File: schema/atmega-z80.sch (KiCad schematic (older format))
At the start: 68 parts, among them J1 USB Connector, J2 Programmer ISP 10, J3 SPI Connector, J4 I2C Connector, Q1 PNP_2N4403, Q2 PNP_2N4403, Q3 NPN_2N4401, Q4 PNP_2N4403, U1 Z84C0010PEG, U2 ATmega324A-PU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

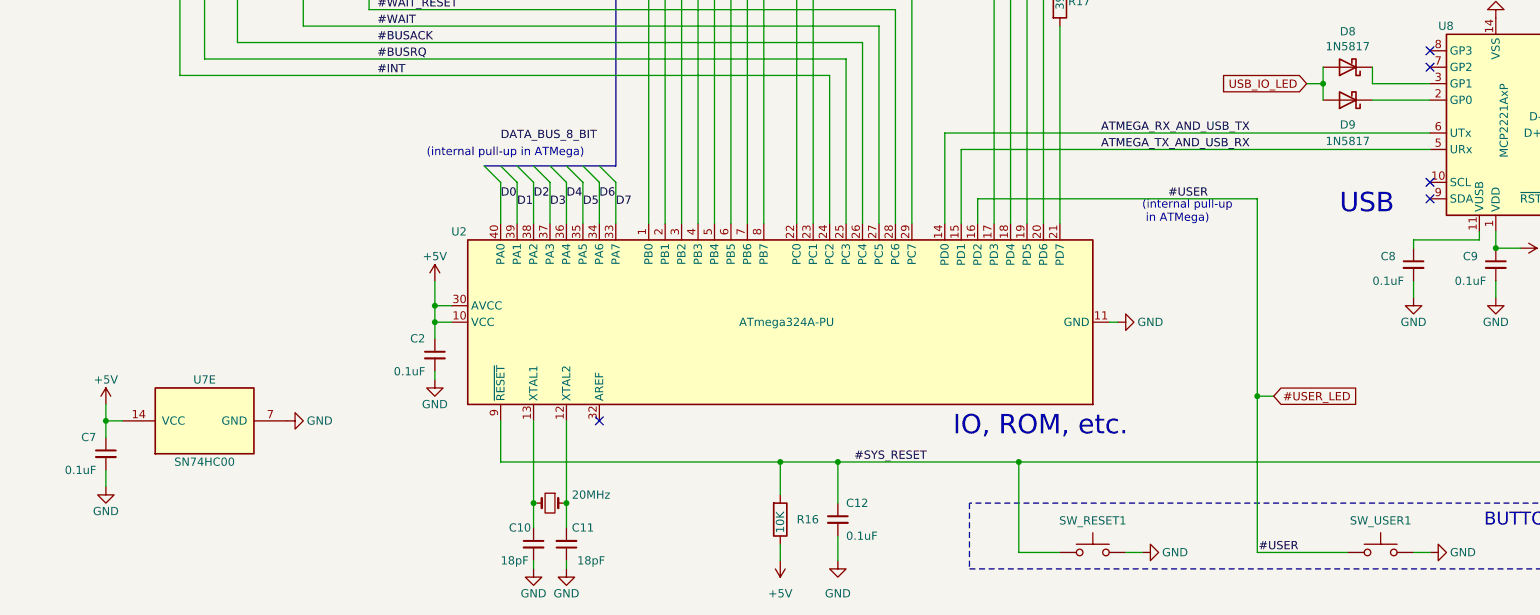
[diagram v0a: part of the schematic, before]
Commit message: A bunch of improvements / additions (#5)
* A bunch of improvements / additions
- PCB layout improvements
- 1N5817 diode datasheet
- CMake support
- ATMega program loader firmware
- program loader tool (z80_prog_loader.py)
- Z80 bootloader (bootloader.asm)
- Z80 sample program (blinky.asm)
- goose logo! (goose-icon.kicad_mod)
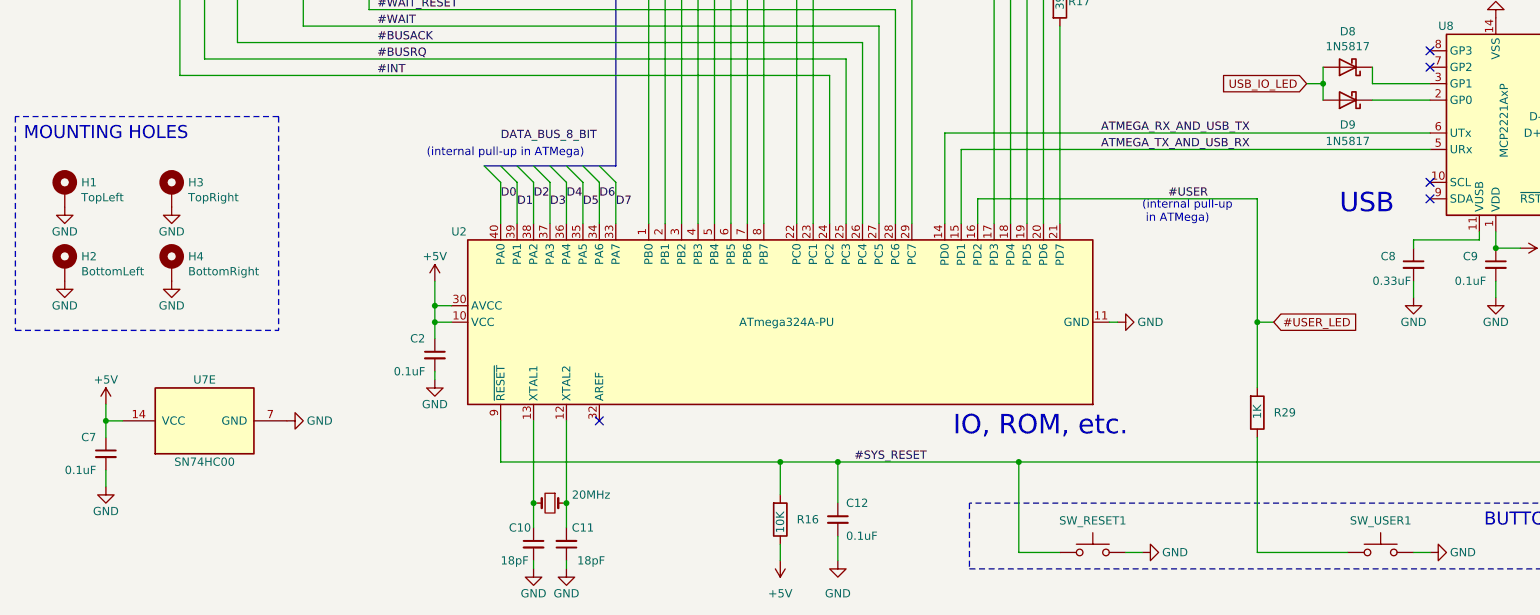
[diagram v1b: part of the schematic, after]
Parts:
- added H1: TopLeft, MountingHole:MountingHole_2.2mm_M2_DIN965_Pad, symbol Mechanical:MountingHole_Pad
- added H2: BottomLeft, MountingHole:MountingHole_2.2mm_M2_DIN965_Pad, symbol Mechanical:MountingHole_Pad
- added H3: TopRight, MountingHole:MountingHole_2.2mm_M2_DIN965_Pad, symbol Mechanical:MountingHole_Pad
- added H4: BottomRight, MountingHole:MountingHole_2.2mm_M2_DIN965_Pad, symbol Mechanical:MountingHole_Pad
- added R29: 1K, Resistor_SMD:R_1206_3216Metric_Pad1.30x1.75mm_HandSolder, symbol Device:R
- C8: value 0.1uF -> 0.33uF
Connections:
- net #USER_LED: now also R29.2; no longer SW_USER1.1
- net GND: now also H1.1, H2.1, H3.1, H4.1
- new net: R29.1, SW_USER1.1
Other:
- note added: "MOUNTING HOLES"
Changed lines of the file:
@@
 Text Label 7850 8700 2    50   ~ 0
-#USER
-Text Label 8400 10850 2    50   ~ 0
 #USER
 Text GLabel 1400 3700 0    50   Input ~ 0
@@
 P 9100 9100
 F 0 "C8" H 8900 9150 50  0000 L CNN
-F 1 "0.1uF" H 8850 9000 50  0000 L CNN
+F 1 "0.33uF" H 8850 9000 50  0000 L CNN
 F 2 "Capacitor_SMD:C_1206_3216Metric_Pad1.33x1.80mm_HandSolder" H 9100 9100 50  0001 C CNN
 F 3 "~" H 9100 9100 50  0001 C CNN
@@
 Wire Wire Line
 	10000 8300 12150 8300
-Text GLabel 8250 9900 2    50   Input ~ 0
+Text GLabel 8250 9450 2    50   Input ~ 0
 #USER_LED
 Wire Wire Line
-	8250 9900 8150 9900
+	8250 9450 8150 9450
 Wire Wire Line
 	6700 10850 6950 10850
 Wire Wire Line
 	6700 10850 6700 10300
-Connection ~ 8150 9900
-Wire Wire Line
-	8150 9900 8150 10850
-Wire Wire Line
-	8150 8700 8150 9900
+Wire Wire Line
+	8150 8700 8150 9450
 Text Notes 7450 8850 0    50   ~ 0
 (internal pull-up\n in ATMega)
@@
 	0    -1   -1   0
 $EndComp
+$Comp
+L Mechanical:MountingHole_Pad H1
+U 1 1 614CF04A
+P 900 8650
+F 0 "H1" H 1000 8699 50  0000 L CNN
+F 1 "TopLeft" H 1000 8608 50  0000 L CNN
+F 2 "MountingHole:MountingHole_2.2mm_M2_DIN965_Pad" H 900 8650 50  0001 C CNN
+F 3 "~" H 900 8650 50  0001 C CNN
+	1    900  8650
+	1    0    0    -1
+$EndComp
+$Comp
+L Mechanical:MountingHole_Pad H3
+U 1 1 614CFF48
+P 1550 8650
+F 0 "H3" H 1650 8699 50  0000 L CNN
+F 1 "TopRight" H 1650 8608 50  0000 L CNN
+F 2 "MountingHole:MountingHole_2.2mm_M2_DIN965_Pad" H 1550 8650 50  0001 C CNN
+F 3 "~" H 1550 8650 50  0001 C CNN
+	1    1550 8650
+	1    0    0    -1
+$EndComp
+$Comp
+L Mechanical:MountingHole_Pad H2
+U 1 1 614D03BD
+P 900 9100
+F 0 "H2" H 1000 9149 50  0000 L CNN
+F 1 "BottomLeft" H 1000 9058 50  0000 L CNN
+F 2 "MountingHole:MountingHole_2.2mm_M2_DIN965_Pad" H 900 9100 50  0001 C CNN
+F 3 "~" H 900 9100 50  0001 C CNN
+	1    900  9100
+	1    0    0    -1
+$EndComp
+$Comp
+L power:GND #PWR01
+U 1 1 614D164C
+P 900 8750
+F 0 "#PWR01" H 900 8500 50  0001 C CNN
+F 1 "GND" H 900 8600 50  0000 C CNN
+F 2 "" H 900 8750 50  0001 C CNN
+F 3 "" H 900 8750 50  0001 C CNN
+	1    900  8750
+	1    0    0    -1
+$EndComp
+$Comp
+L power:GND #PWR02
+U 1 1 614D21D8
+P 900 9200
+F 0 "#PWR02" H 900 8950 50  0001 C CNN
+F 1 "GND" H 900 9050 50  0000 C CNN
+F 2 "" H 900 9200 50  0001 C CNN
+F 3 "" H 900 9200 50  0001 C CNN
+	1    900  9200
+	1    0    0    -1
+$EndComp
+$Comp
+L power:GND #PWR03
+U 1 1 614D26A2
+P 1550 8750
+F 0 "#PWR03" H 1550 8500 50  0001 C CNN
+F 1 "GND" H 1550 8600 50  0000 C CNN
+F 2 "" H 1550 8750 50  0001 C CNN
+F 3 "" H 1550 8750 50  0001 C CNN
+	1    1550 8750
+	1    0    0    -1
+$EndComp
+$Comp
+L power:GND #PWR04
+U 1 1 614D2B35
+P 1550 9200
+F 0 "#PWR04" H 1550 8950 50  0001 C CNN
+F 1 "GND" H 1550 9050 50  0000 C CNN
+F 2 "" H 1550 9200 50  0001 C CNN
+F 3 "" H 1550 9200 50  0001 C CNN
+	1    1550 9200
+	1    0    0    -1
+$EndComp
+$Comp
+L Mechanical:MountingHole_Pad H4
+U 1 1 614D0773
+P 1550 9100
+F 0 "H4" H 1650 9149 50  0000 L CNN
+F 1 "BottomRight" H 1650 9058 50  0000 L CNN
+F 2 "MountingHole:MountingHole_2.2mm_M2_DIN965_Pad" H 1550 9100 50  0001 C CNN
+F 3 "~" H 1550 9100 50  0001 C CNN
+	1    1550 9100
+	1    0    0    -1
+$EndComp
+Wire Notes Line
+	600  9500 2200 9500
+Wire Notes Line
+	2200 8200 600  8200
+Wire Notes Line
+	2200 8200 2200 9500
+Wire Notes Line
+	600  8200 600  9500
+Text Notes 650  8350 0    79   ~ 0
+MOUNTING HOLES
+$Comp
+L Device:R R29
+U 1 1 61510E7E
+P 8150 10000
+F 0 "R29" H 8250 10000 50  0000 L CNN
+F 1 "1K" V 8150 9950 50  0000 L CNN
+F 2 "Resistor_SMD:R_1206_3216Metric_Pad1.30x1.75mm_HandSolder" V 8080 10000 50  0001 C CNN
+F 3 "~" H 8150 10000 50  0001 C CNN
+	1    8150 10000
+	1    0    0    1
+$EndComp
+Wire Wire Line
+	8150 9450 8150 9850
+Connection ~ 8150 9450
+Wire Wire Line
+	8150 10150 8150 10850
 Wire Bus Line
 	8550 2100 8550 3250

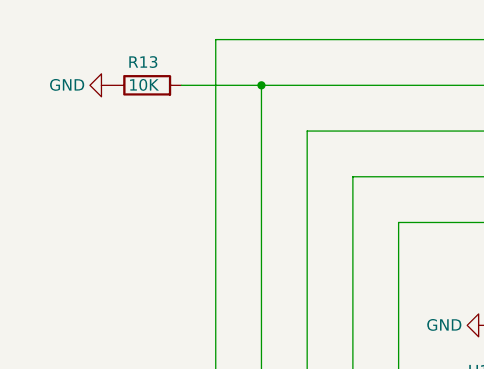
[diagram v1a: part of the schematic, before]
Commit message: Changed #Z80_RESET line pull-down (R13) to pull-up
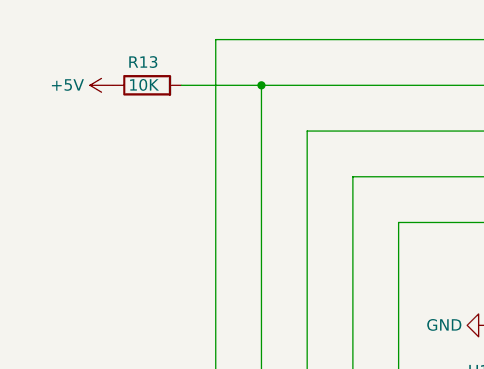
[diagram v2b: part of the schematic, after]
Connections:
- net +5V: now also R13.1
- net GND: no longer R13.1
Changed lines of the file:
@@
 Text Notes 3100 8450 0    50   ~ 0
 (internal pull-up in ATMega)
-$Comp
-L power:GND #PWR0150
-U 1 1 617B67AE
-P 1000 950
-F 0 "#PWR0150" H 1000 700 50  0001 C CNN
-F 1 "GND" V 1000 750 50  0000 C CNN
-F 2 "" H 1000 950 50  0001 C CNN
-F 3 "" H 1000 950 50  0001 C CNN
-	1    1000 950
-	0    1    1    0
-$EndComp
 Wire Wire Line
 	1850 1150 1850 4300
@@
 Wire Bus Line
 	5250 2100 5250 5600
+$Comp
+L power:+5V #PWR0150
+U 1 1 61559FBB
+P 1000 950
+F 0 "#PWR0150" H 1000 800 50  0001 C CNN
+F 1 "+5V" V 1000 1150 50  0000 C CNN
+F 2 "" H 1000 950 50  0001 C CNN
+F 3 "" H 1000 950 50  0001 C CNN
+	1    1000 950
+	0    -1   -1   0
+$EndComp
 $EndSCHEMATC

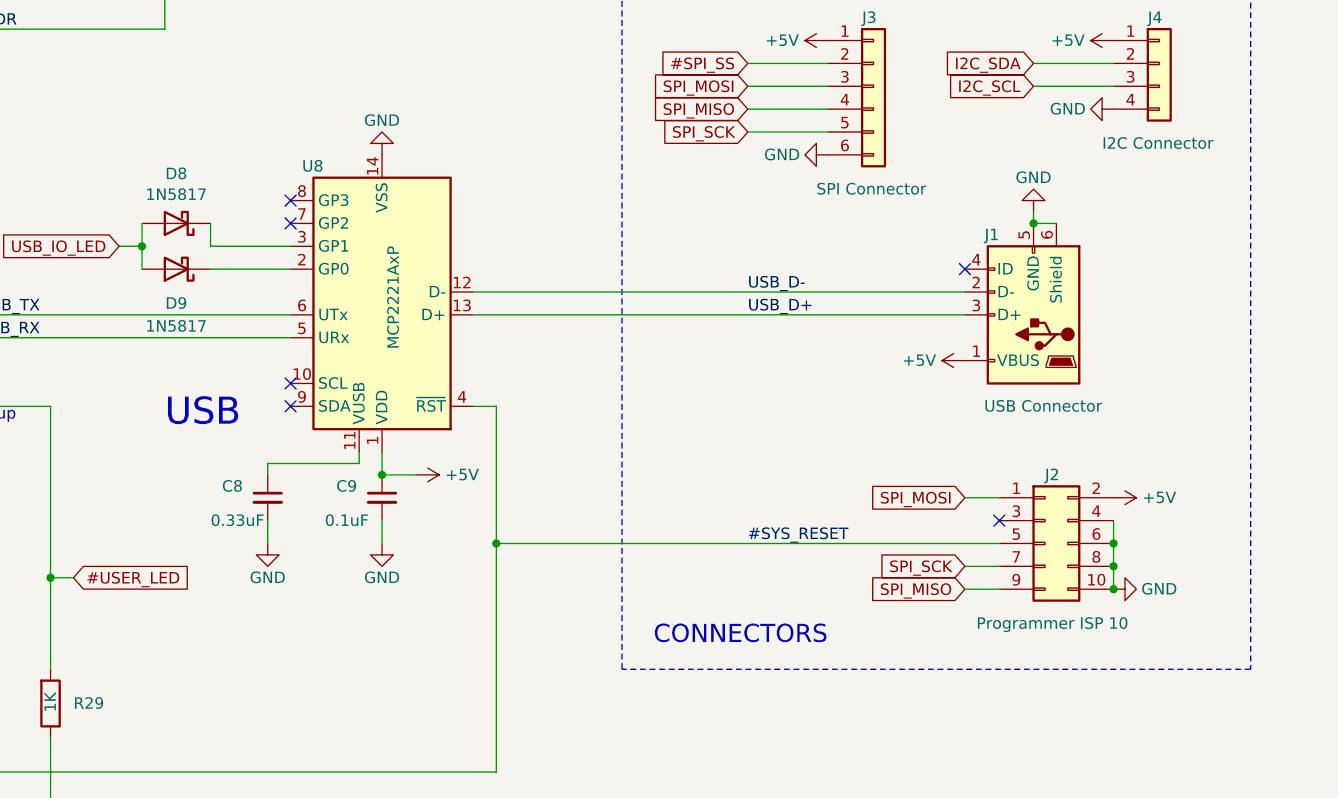
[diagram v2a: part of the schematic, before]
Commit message: Improvements and bugfixes (#7)
Small improvements and bugfixes

- USART timeout checks during Z80 code upload
- error codes are now returned during Z80 code upload instead of a single ACK/NACK
- added own implementation of mcp2221 python library due to a bug in the official one
- updated atmega-z80.pdf
- minor PCB improvements
- other small bugfixes in z80_prog_loader.py and blinky.asm
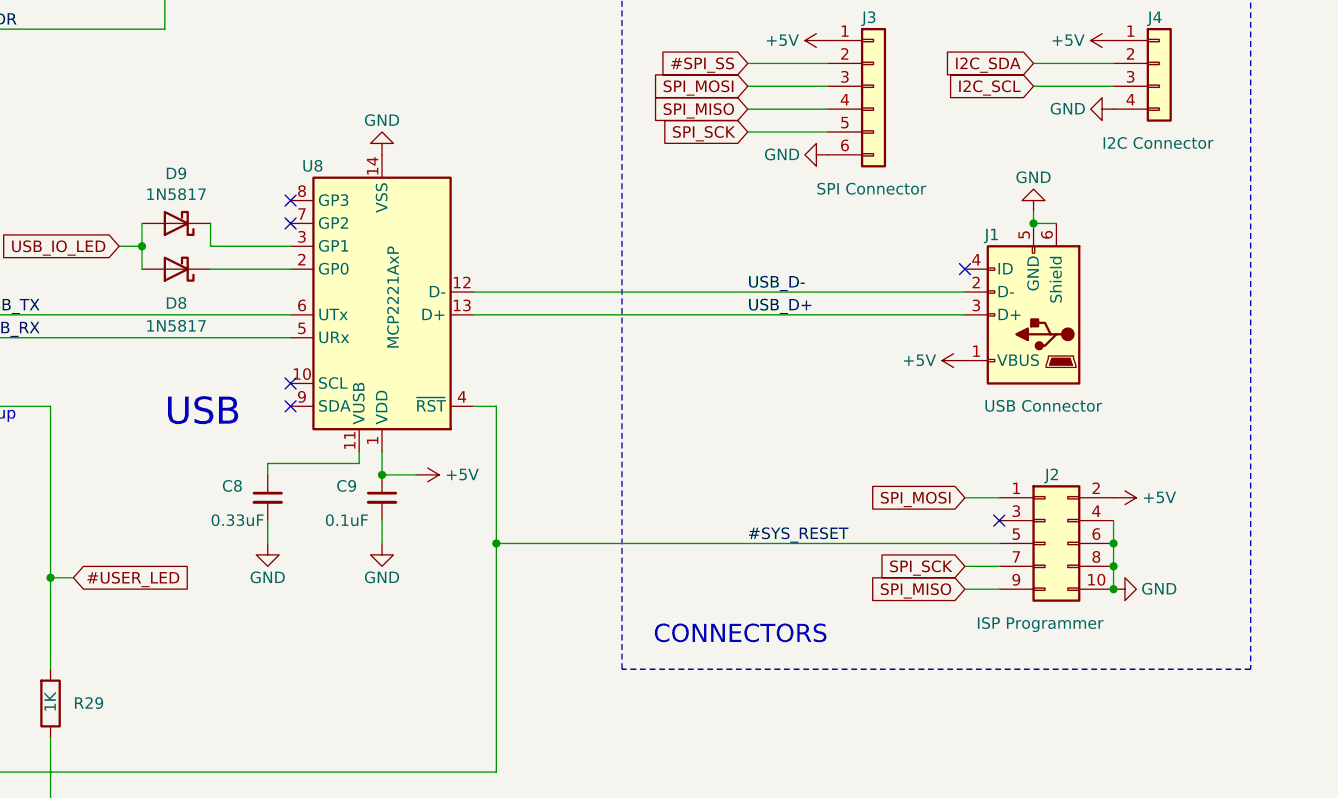
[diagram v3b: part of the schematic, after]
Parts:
- J2: value Programmer ISP 10 -> ISP Programmer
- SW_RESET1: value SW_Push -> RESET
- SW_USER1: value SW_Push -> USER
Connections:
- net at U8.2 (GP0): now also D8.1 (K); no longer D9.1 (K)
- net at U8.3 (GP1): now also D9.1 (K); no longer D8.1 (K)
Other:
- moved on the sheet: D8, D9
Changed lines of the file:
@@
 Wire Wire Line
 	3150 9450 3150 9550
-$Comp
-L Switch:SW_Push SW_USER1
-U 1 1 62362542
-P 8900 10850
-F 0 "SW_USER1" H 8900 11043 50  0000 C CNN
-F 1 "SW_Push" H 8900 11044 50  0001 C CNN
-F 2 "Button_Switch_THT:SW_PUSH_6mm_H5mm" H 8900 11050 50  0001 C CNN
-F 3 "~" H 8900 11050 50  0001 C CNN
-	1    8900 10850
-	1    0    0    -1
-$EndComp
 Wire Wire Line
 	9200 10850 9100 10850
@@
 Wire Wire Line
 	3750 10900 3750 10950
-$Comp
-L Switch:SW_Push SW_RESET1
-U 1 1 625E0418
-P 7150 10850
-F 0 "SW_RESET1" H 7150 11043 50  0000 C CNN
-F 1 "SW_Push" H 7150 11044 50  0001 C CNN
-F 2 "Button_Switch_THT:SW_PUSH_6mm_H5mm" H 7150 11050 50  0001 C CNN
-F 3 "~" H 7150 11050 50  0001 C CNN
-	1    7150 10850
-	-1   0    0    -1
-$EndComp
 $Comp
 L power:+5V #PWR0108
@@
 Text GLabel 15250 4550 2    50   Input ~ 0
 USB_IO_LED
-$Comp
-L Device:LED_ALT D1
-U 1 1 61EB9A16
-P 15000 4550
-F 0 "D1" H 14900 4400 50  0000 C CNN
-F 1 "LED_USB_IO" H 14993 4676 50  0000 C CNN
-F 2 "LED_THT:LED_D5.0mm" H 15000 4550 50  0001 C CNN
-F 3 "~" H 15000 4550 50  0001 C CNN
-	1    15000 4550
-	-1   0    0    -1
-$EndComp
 Wire Wire Line
 	15150 5050 15250 5050
@@
 P 12500 9300
 F 0 "J2" H 12500 9600 50  0000 L CNN
-F 1 "Programmer ISP 10" H 12200 8950 50  0000 L CNN
+F 1 "ISP Programmer" H 12200 8950 50  0000 L CNN
 F 2 "Connector_PinHeader_2.54mm:PinHeader_2x05_P2.54mm_Vertical" H 12500 9300 50  0001 C CNN
 F 3 "~" H 12500 9300 50  0001 C CNN
@@
 L Diode:1N5817 D9
 U 1 1 61418E5F
+P 8700 7900
+F 0 "D9" H 8700 7683 50  0000 C CNN
+F 1 "1N5817" H 8700 7774 50  0000 C CNN
+F 2 "Diode_THT:D_DO-41_SOD81_P10.16mm_Horizontal" H 8700 7725 50  0001 C CNN
+F 3 "http://www.vishay.com/docs/88525/1n5817.pdf" H 8700 7900 50  0001 C CNN
+	1    8700 7900
+	-1   0    0    1
+$EndComp
+$Comp
+L Diode:1N5817 D8
+U 1 1 6141BB94
 P 8700 8100
-F 0 "D9" H 8700 8250 50  0000 C CNN
+F 0 "D8" H 8700 8250 50  0000 C CNN
 F 1 "1N5817" H 8700 8350 50  0000 C CNN
 F 2 "Diode_THT:D_DO-41_SOD81_P10.16mm_Horizontal" H 8700 7925 50  0001 C CNN
 F 3 "http://www.vishay.com/docs/88525/1n5817.pdf" H 8700 8100 50  0001 C CNN
 	1    8700 8100
-	-1   0    0    1
-$EndComp
-$Comp
-L Diode:1N5817 D8
-U 1 1 6141BB94
-P 8700 7900
-F 0 "D8" H 8700 7683 50  0000 C CNN
-F 1 "1N5817" H 8700 7774 50  0000 C CNN
-F 2 "Diode_THT:D_DO-41_SOD81_P10.16mm_Horizontal" H 8700 7725 50  0001 C CNN
-F 3 "http://www.vishay.com/docs/88525/1n5817.pdf" H 8700 7900 50  0001 C CNN
-	1    8700 7900
 	-1   0    0    1
 $EndComp
@@
 Wire Wire Line
 	8150 10150 8150 10850
+$Comp
+L power:+5V #PWR0150
+U 1 1 61559FBB
+P 1000 950
+F 0 "#PWR0150" H 1000 800 50  0001 C CNN
+F 1 "+5V" V 1000 1150 50  0000 C CNN
+F 2 "" H 1000 950 50  0001 C CNN
+F 3 "" H 1000 950 50  0001 C CNN
+	1    1000 950
+	0    -1   -1   0
+$EndComp
 Wire Bus Line
 	8550 2100 8550 3250
@@
 	5250 2100 5250 5600
 $Comp
-L power:+5V #PWR0150
-U 1 1 61559FBB
-P 1000 950
-F 0 "#PWR0150" H 1000 800 50  0001 C CNN
-F 1 "+5V" V 1000 1150 50  0000 C CNN
-F 2 "" H 1000 950 50  0001 C CNN
-F 3 "" H 1000 950 50  0001 C CNN
-	1    1000 950
-	0    -1   -1   0
+L Device:LED_ALT D1
+U 1 1 61EB9A16
+P 15000 4550
+F 0 "D1" H 14900 4400 50  0000 C CNN
+F 1 "LED_USB_IO" H 14993 4676 50  0000 C CNN
+F 2 "LED_THT:LED_D5.0mm" H 15000 4550 50  0001 C CNN
+F 3 "~" H 15000 4550 50  0001 C CNN
+	1    15000 4550
+	-1   0    0    -1
+$EndComp
+$Comp
+L Switch:SW_Push SW_USER1
+U 1 1 62362542
+P 8900 10850
+F 0 "SW_USER1" H 8900 11043 50  0000 C CNN
+F 1 "USER" H 8900 11044 50  0001 C CNN
+F 2 "Button_Switch_THT:SW_PUSH_6mm_H5mm" H 8900 11050 50  0001 C CNN
+F 3 "~" H 8900 11050 50  0001 C CNN
+	1    8900 10850
+	1    0    0    -1
+$EndComp
+$Comp
+L Switch:SW_Push SW_RESET1
+U 1 1 625E0418
+P 7150 10850
+F 0 "SW_RESET1" H 7150 11043 50  0000 C CNN
+F 1 "RESET" H 7150 11044 50  0001 C CNN
+F 2 "Button_Switch_THT:SW_PUSH_6mm_H5mm" H 7150 11050 50  0001 C CNN
+F 3 "~" H 7150 11050 50  0001 C CNN
+	1    7150 10850
+	-1   0    0    -1
 $EndComp
 $EndSCHEMATC
